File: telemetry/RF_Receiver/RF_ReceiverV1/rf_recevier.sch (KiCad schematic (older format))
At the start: 21 parts, among them J1 USB_B, J3 CONN_02X03, U1 FT231XS, U3 ATmega328P-AU, Y1 Crystal_SMD

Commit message: basic changes to schematic, still more to do
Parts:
- removed C11, C12: C_30pF, footprints:C_0805_OEM, symbol rf_recevier-rescue:C_30pF-formula-benji_arduino2-rescue
- removed C2, C5: C_0.1uF, footprints:C_0805_OEM, symbol rf_recevier-rescue:C_0.1uF-formula-benji_arduino2-rescue
- removed C3: C_100nF, footprints:C_0603_1608Metric, symbol rf_recevier-rescue:C_100nF-formula-benji_arduino2-rescue
- removed D2, D4, D7, D8: LED, symbol Device:LED
- removed F1: F_500mA_16V, footprints:Fuse_1210, symbol rf_recevier-rescue:F_500mA_16V-formula-benji_arduino2-rescue
- removed J1: USB_B, symbol rf_recevier-rescue:USB_B-Connector-benji_arduino2-rescue
- removed J3: CONN_02X03, footprints:Pin_Header_Straight_2x03, symbol rf_recevier-rescue:CONN_02X03-formula-benji_arduino2-rescue
- removed R2, R3, R6, R7, R8, R9: R_1K, footprints:R_0805_OEM, symbol rf_recevier-rescue:R_1K-formula-benji_arduino2-rescue
- removed U1: FT231XS, Package_SO:SSOP-20_3.9x8.7mm_P0.635mm, symbol Interface_USB:FT231XS
- removed U3: ATmega328P-AU, Package_QFP:TQFP-32_7x7mm_P0.8mm, symbol rf_recevier-rescue:ATmega328P-AU-formula-benji_arduino2-rescue
- removed Y1: Crystal_SMD, footprints:Crystal_SMD_FA238, symbol rf_recevier-rescue:Crystal_SMD-formula-benji_arduino2-rescue
- added C? (x2): C_0.1uF, footprints:C_0805_OEM, symbol Formula:C_0.1uF
- added C?: C_100nF, footprints:C_0603_1608Metric, symbol Formula:C_100nF
- added C? (x2): C_30pF, footprints:C_0805_OEM, symbol Formula:C_30pF
- added D?: LED_0805_PB0, footprints:LED_0805_OEM, symbol Formula:LED_0805
- added D? (x2): LED_0805, footprints:LED_0805_OEM, symbol Formula:LED_0805
- added D?: LED_0805_PB5, footprints:LED_0805_OEM, symbol Formula:LED_0805
- added F?: F_500mA_16V, footprints:Fuse_1210, symbol Formula:F_500mA_16V
- added J?: USB_A, symbol Formula:USB_A
- added J?: 0.1in_Female_Socket_01x16, Connector_PinSocket_2.54mm:PinSocket_1x16_P2.54mm_Vertical, symbol Formula:0.1in_Female_Socket_01x16
- added J?: CONN_02X03, footprints:Pin_Header_Straight_2x03, symbol Formula:CONN_02X03
- added R? (x4): R_1K, footprints:R_0805_OEM, symbol Formula:R_1K
- added R? (x2): R_200, footprints:R_0805_OEM, symbol Formula:R_200
- added U?: ATmega328P-AU, Package_QFP:TQFP-32_7x7mm_P0.8mm, symbol Formula:ATmega328P-AU
- added U?: FT232RL, Package_SO:SSOP-28_5.3x10.2mm_P0.65mm, symbol Formula:FT232RL
- added Y?: Crystal_SMD, footprints:Crystal_SMD_FA238, symbol Formula:Crystal_SMD
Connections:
- net labels added: 104, 105, 106, 107, 3v3_FTDI, DEBUG_LED, USB_RX, USB_TX, VBATT
- net labels removed: +5V, 3V3_FTDI, IO4, IO5, IO6, IO7, IO8, Rx, Tx
- wire segments 63 -> 62
- no-connect marks 12 -> 15
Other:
- note added: "LCD Screen Connection"

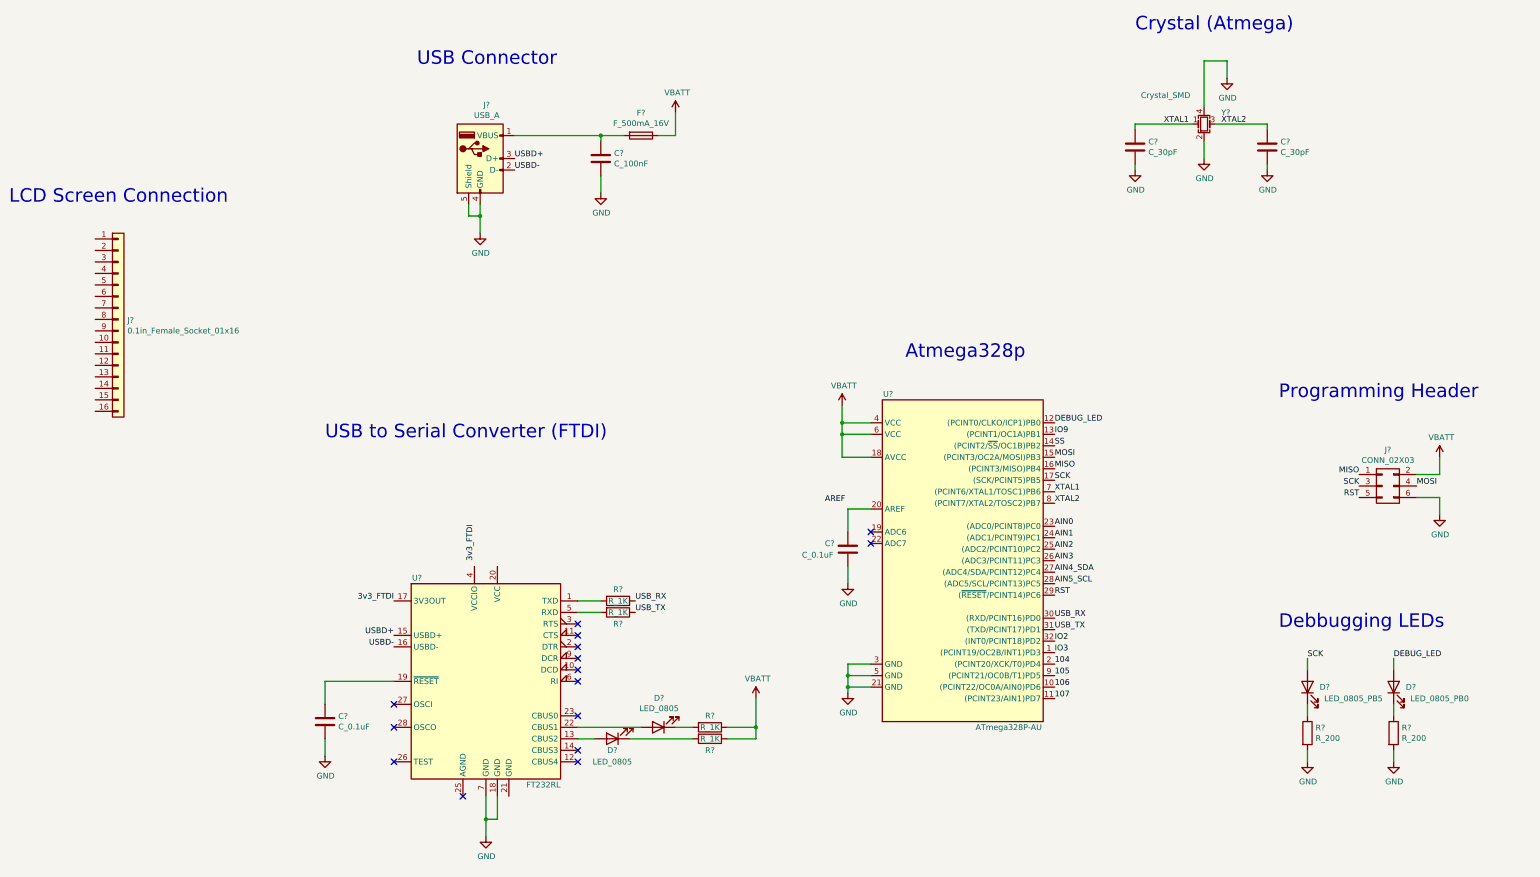
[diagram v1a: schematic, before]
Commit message: added annotations
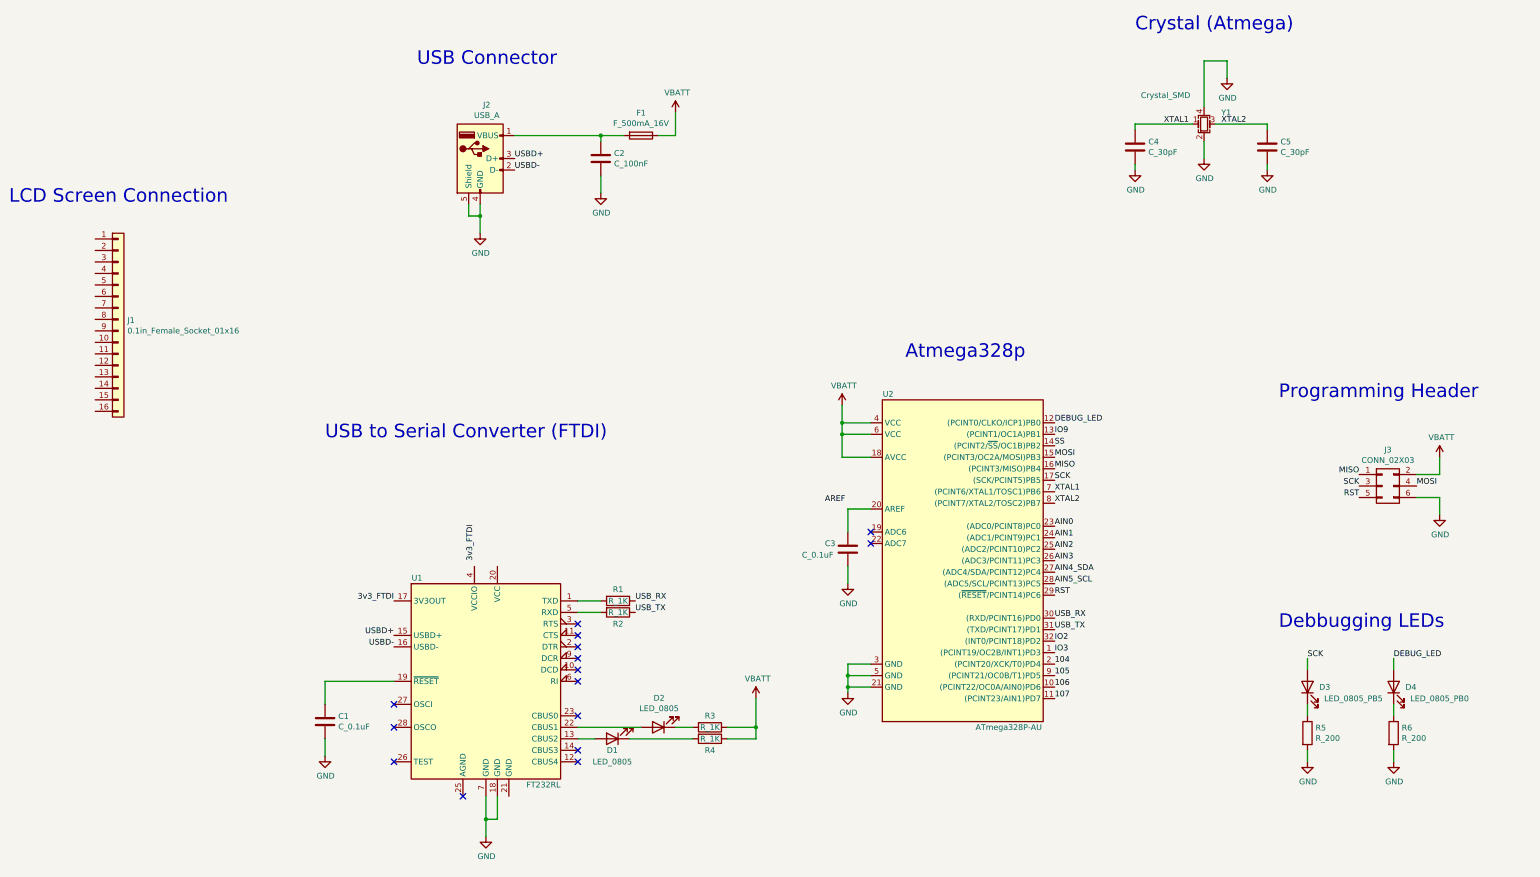
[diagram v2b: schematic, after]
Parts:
- gave numbers to parts that had none: 22
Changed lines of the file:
@@
 USB Connector
 $Comp
-L Formula:FT232RL U?
+L Formula:FT232RL U1
 U 1 1 5FBB1322
 P 5350 7200
-F 0 "U?" H 4750 8100 50  0000 C CNN
+F 0 "U1" H 4750 8100 50  0000 C CNN
 F 1 "FT232RL" H 5850 6300 50  0000 C CNN
 F 2 "Package_SO:SSOP-28_5.3x10.2mm_P0.65mm" H 6450 6300 50  0001 C CNN
@@
 $EndComp
 $Comp
-L Formula:USB_A J?
+L Formula:USB_A J2
 U 1 1 5FBBADA0
 P 5300 2650
-F 0 "J?" H 5357 3117 50  0000 C CNN
+F 0 "J2" H 5357 3117 50  0000 C CNN
 F 1 "USB_A" H 5357 3026 50  0000 C CNN
 F 2 "" H 5450 2600 50  0001 C CNN
@@
 $EndComp
 $Comp
-L Formula:0.1in_Female_Socket_01x16 J?
+L Formula:0.1in_Female_Socket_01x16 J1
 U 1 1 5FBD5439
 P 2150 4050
-F 0 "J?" H 2230 4042 50  0000 L CNN
+F 0 "J1" H 2230 4042 50  0000 L CNN
 F 1 "0.1in_Female_Socket_01x16" H 2230 3951 50  0000 L CNN
 F 2 "Connector_PinSocket_2.54mm:PinSocket_1x16_P2.54mm_Vertical" H 2050 4750 50  0001 C CNN
@@
 $EndComp
 $Comp
-L Formula:CONN_02X03 J?
+L Formula:CONN_02X03 J3
 U 1 1 5FBD8D61
 P 13200 5500
-F 0 "J?" H 13200 5815 50  0000 C CNN
+F 0 "J3" H 13200 5815 50  0000 C CNN
 F 1 "CONN_02X03" H 13200 5724 50  0000 C CNN
 F 2 "footprints:Pin_Header_Straight_2x03" H 13200 4300 50  0001 C CNN
@@
 	3950 7200 3950 7400
 $Comp
-L Formula:VBATT #PWR?
+L Formula:VBATT #PWR07
 U 1 1 5FBF11C9
 P 8450 4800
-F 0 "#PWR?" H 8450 4650 50  0001 C CNN
+F 0 "#PWR07" H 8450 4650 50  0001 C CNN
 F 1 "VBATT" H 8465 4973 50  0000 C CNN
 F 2 "" H 8450 4800 50  0001 C CNN
@@
 	3950 7700 3950 7850
 $Comp
-L power:GND #PWR?
+L power:GND #PWR01
 U 1 1 5FC0F959
 P 3950 7850
-F 0 "#PWR?" H 3950 7600 50  0001 C CNN
+F 0 "#PWR01" H 3950 7600 50  0001 C CNN
 F 1 "GND" H 3955 7677 50  0000 C CNN
 F 2 "" H 3950 7850 50  0001 C CNN
@@
 $EndComp
 $Comp
-L Formula:C_0.1uF C?
+L Formula:C_0.1uF C1
 U 1 1 5FBA02F3
 P 3950 7550
-F 0 "C?" H 4065 7596 50  0000 L CNN
+F 0 "C1" H 4065 7596 50  0000 L CNN
 F 1 "C_0.1uF" H 4065 7505 50  0000 L CNN
 F 2 "footprints:C_0805_OEM" H 3988 7400 50  0001 C CNN
@@
 	8450 5050 8450 4950
 $Comp
-L Formula:VBATT #PWR?
+L Formula:VBATT #PWR06
 U 1 1 5FBCF49A
 P 7700 7350
-F 0 "#PWR?" H 7700 7200 50  0001 C CNN
+F 0 "#PWR06" H 7700 7200 50  0001 C CNN
 F 1 "VBATT" H 7715 7523 50  0000 C CNN
 F 2 "" H 7700 7350 50  0001 C CNN
@@
 3v3_FTDI
 $Comp
-L Formula:R_1K R?
+L Formula:R_1K R3
 U 1 1 5FBDE1F0
 P 7300 7600
-F 0 "R?" V 7200 7600 50  0000 C CNN
+F 0 "R3" V 7200 7600 50  0000 C CNN
 F 1 "R_1K" V 7300 7600 50  0000 C CNN
 F 2 "footprints:R_0805_OEM" H 7230 7600 50  0001 C CNN
@@
 $EndComp
 $Comp
-L Formula:R_1K R?
+L Formula:R_1K R4
 U 1 1 5FBE3B53
 P 7300 7700
-F 0 "R?" V 7400 7700 50  0000 C CNN
+F 0 "R4" V 7400 7700 50  0000 C CNN
 F 1 "R_1K" V 7300 7700 50  0000 C CNN
 F 2 "footprints:R_0805_OEM" H 7230 7700 50  0001 C CNN
@@
 $EndComp
 $Comp
-L Formula:LED_0805 D?
+L Formula:LED_0805 D1
 U 1 1 5FBD99DF
 P 6450 7700
-F 0 "D?" H 6450 7800 50  0000 C CNN
+F 0 "D1" H 6450 7800 50  0000 C CNN
 F 1 "LED_0805" H 6450 7900 50  0000 C CNN
 F 2 "footprints:LED_0805_OEM" H 6350 7700 50  0001 C CNN
@@
 $EndComp
 $Comp
-L Formula:LED_0805 D?
+L Formula:LED_0805 D2
 U 1 1 5FBD7332
 P 6850 7600
-F 0 "D?" H 6843 7345 50  0000 C CNN
+F 0 "D2" H 6843 7345 50  0000 C CNN
 F 1 "LED_0805" H 6843 7436 50  0000 C CNN
 F 2 "footprints:LED_0805_OEM" H 6750 7600 50  0001 C CNN
@@
 	7700 7600 7700 7700
 $Comp
-L Formula:R_1K R?
+L Formula:R_1K R1
 U 1 1 5FC279C9
 P 6500 6500
-F 0 "R?" V 6400 6500 50  0000 C CNN
+F 0 "R1" V 6400 6500 50  0000 C CNN
 F 1 "R_1K" V 6500 6500 50  0000 C CNN
 F 2 "footprints:R_0805_OEM" H 6430 6500 50  0001 C CNN
@@
 $EndComp
 $Comp
-L Formula:R_1K R?
+L Formula:R_1K R2
 U 1 1 5FC279D2
 P 6500 6600
-F 0 "R?" V 6600 6600 50  0000 C CNN
+F 0 "R2" V 6600 6600 50  0000 C CNN
 F 1 "R_1K" V 6500 6600 50  0000 C CNN
 F 2 "footprints:R_0805_OEM" H 6430 6600 50  0001 C CNN
@@
 Connection ~ 5300 3150
 $Comp
-L power:GND #PWR?
+L power:GND #PWR03
 U 1 1 5FC02331
 P 5350 8550
-F 0 "#PWR?" H 5350 8300 50  0001 C CNN
+F 0 "#PWR03" H 5350 8300 50  0001 C CNN
 F 1 "GND" H 5355 8377 50  0000 C CNN
 F 2 "" H 5350 8550 50  0001 C CNN
@@
 $EndComp
 $Comp
-L power:GND #PWR?
+L power:GND #PWR02
 U 1 1 5FC3F217
 P 5300 3300
-F 0 "#PWR?" H 5300 3050 50  0001 C CNN
+F 0 "#PWR02" H 5300 3050 50  0001 C CNN
 F 1 "GND" H 5305 3127 50  0000 C CNN
 F 2 "" H 5300 3300 50  0001 C CNN
@@
 Connection ~ 6350 2450
 $Comp
-L Formula:C_100nF C?
+L Formula:C_100nF C2
 U 1 1 5FC4DEA7
 P 6350 2650
-F 0 "C?" H 6465 2696 50  0000 L CNN
+F 0 "C2" H 6465 2696 50  0000 L CNN
 F 1 "C_100nF" H 6465 2605 50  0000 L CNN
 F 2 "footprints:C_0603_1608Metric" H 6388 2500 50  0001 C CNN
@@
 $EndComp
 $Comp
-L power:GND #PWR?
+L power:GND #PWR04
 U 1 1 5FC4F35A
 P 6350 2950
-F 0 "#PWR?" H 6350 2700 50  0001 C CNN
+F 0 "#PWR04" H 6350 2700 50  0001 C CNN
 F 1 "GND" H 6355 2777 50  0000 C CNN
 F 2 "" H 6350 2950 50  0001 C CNN
@@
 $EndComp
 $Comp
-L Formula:VBATT #PWR?
+L Formula:VBATT #PWR05
 U 1 1 5FC5813F
 P 7000 2250
-F 0 "#PWR?" H 7000 2100 50  0001 C CNN
+F 0 "#PWR05" H 7000 2100 50  0001 C CNN
 F 1 "VBATT" H 7015 2423 50  0000 C CNN
 F 2 "" H 7000 2250 50  0001 C CNN
@@
 $EndComp
 $Comp
-L Formula:F_500mA_16V F?
+L Formula:F_500mA_16V F1
 U 1 1 5FC59506
 P 6700 2450
-F 0 "F?" V 6503 2450 50  0000 C CNN
+F 0 "F1" V 6503 2450 50  0000 C CNN
 F 1 "F_500mA_16V" V 6594 2450 50  0000 C CNN
 F 2 "footprints:Fuse_1210" V 6630 2450 50  0001 C CNN
@@
 	6350 2800 6350 2950
 $Comp
-L power:GND #PWR?
+L power:GND #PWR012
 U 1 1 5FC6FC40
 P 11800 1950
-F 0 "#PWR?" H 11800 1700 50  0001 C CNN
+F 0 "#PWR012" H 11800 1700 50  0001 C CNN
 F 1 "GND" H 11805 1777 50  0000 C CNN
 F 2 "" H 11800 1950 50  0001 C CNN
@@
 $EndComp
 $Comp
-L power:GND #PWR?
+L power:GND #PWR011
 U 1 1 5FC70A2A
 P 11600 2650
-F 0 "#PWR?" H 11600 2400 50  0001 C CNN
+F 0 "#PWR011" H 11600 2400 50  0001 C CNN
 F 1 "GND" H 11605 2477 50  0000 C CNN
 F 2 "" H 11600 2650 50  0001 C CNN
@@
 $EndComp
 $Comp
-L power:GND #PWR?
+L power:GND #PWR010
 U 1 1 5FC71451
 P 11000 2750
-F 0 "#PWR?" H 11000 2500 50  0001 C CNN
+F 0 "#PWR010" H 11000 2500 50  0001 C CNN
 F 1 "GND" H 11005 2577 50  0000 C CNN
 F 2 "" H 11000 2750 50  0001 C CNN
@@
 	11000 2350 11000 2400
 $Comp
-L Formula:C_30pF C?
+L Formula:C_30pF C4
 U 1 1 5FC75CBC
 P 11000 2550
-F 0 "C?" H 11115 2596 50  0000 L CNN
+F 0 "C4" H 11115 2596 50  0000 L CNN
 F 1 "C_30pF" H 11115 2505 50  0000 L CNN
 F 2 "footprints:C_0805_OEM" H 11038 2400 50  0001 C CNN
@@
 	11600 2200 11600 1800
 $Comp
-L Formula:Crystal_SMD Y?
+L Formula:Crystal_SMD Y1
 U 1 1 5FBCF657
 P 11600 2350
-F 0 "Y?" H 11750 2450 50  0000 L CNN
+F 0 "Y1" H 11750 2450 50  0000 L CNN
 F 1 "Crystal_SMD" H 11050 2600 50  0000 L CNN
 F 2 "footprints:Crystal_SMD_FA238" H 11550 2425 50  0001 C CNN
@@
 	11500 2350 11000 2350
 $Comp
-L Formula:C_30pF C?
+L Formula:C_30pF C5
 U 1 1 5FC76DF3
 P 12150 2550
-F 0 "C?" H 12265 2596 50  0000 L CNN
+F 0 "C5" H 12265 2596 50  0000 L CNN
 F 1 "C_30pF" H 12265 2505 50  0000 L CNN
 F 2 "footprints:C_0805_OEM" H 12188 2400 50  0001 C CNN
@@
 	12150 2350 12150 2400
 $Comp
-L power:GND #PWR?
+L power:GND #PWR013
 U 1 1 5FC71E29
 P 12150 2750
-F 0 "#PWR?" H 12150 2500 50  0001 C CNN
+F 0 "#PWR013" H 12150 2500 50  0001 C CNN
 F 1 "GND" H 12155 2577 50  0000 C CNN
 F 2 "" H 12150 2750 50  0001 C CNN
@@
 MOSI
 $Comp
-L Formula:VBATT #PWR?
+L Formula:VBATT #PWR014
 U 1 1 5FC8EFC0
 P 13650 5250
-F 0 "#PWR?" H 13650 5100 50  0001 C CNN
+F 0 "#PWR014" H 13650 5100 50  0001 C CNN
 F 1 "VBATT" H 13665 5423 50  0000 C CNN
 F 2 "" H 13650 5250 50  0001 C CNN
@@
 	13650 5600 13650 5750
 $Comp
-L power:GND #PWR?
+L power:GND #PWR015
 U 1 1 5FC9132A
 P 13650 5750
-F 0 "#PWR?" H 13650 5500 50  0001 C CNN
+F 0 "#PWR015" H 13650 5500 50  0001 C CNN
 F 1 "GND" H 13655 5577 50  0000 C CNN
 F 2 "" H 13650 5750 50  0001 C CNN
@@
 	13450 5600 13650 5600
 $Comp
-L Formula:LED_0805 D?
+L Formula:LED_0805 D4
 U 1 1 5FBD3B41
 P 13250 7250
-F 0 "D?" V 13250 7100 50  0000 C CNN
+F 0 "D4" V 13250 7100 50  0000 C CNN
 F 1 "LED_0805_PB0" V 13150 6850 50  0000 C CNN
 F 2 "footprints:LED_0805_OEM" H 13150 7250 50  0001 C CNN
@@
 $EndComp
 $Comp
-L Formula:LED_0805 D?
+L Formula:LED_0805 D3
 U 1 1 5FCB57F6
 P 12500 7250
-F 0 "D?" V 12500 7100 50  0000 C CNN
+F 0 "D3" V 12500 7100 50  0000 C CNN
 F 1 "LED_0805_PB5" V 12400 6850 50  0000 C CNN
 F 2 "footprints:LED_0805_OEM" H 12400 7250 50  0001 C CNN
@@
 	8500 6200 8500 6350
 $Comp
-L power:GND #PWR?
+L power:GND #PWR08
 U 1 1 5FCD46B7
 P 8500 6350
-F 0 "#PWR?" H 8500 6100 50  0001 C CNN
+F 0 "#PWR08" H 8500 6100 50  0001 C CNN
 F 1 "GND" H 8505 6177 50  0000 C CNN
 F 2 "" H 8500 6350 50  0001 C CNN
@@
 $EndComp
 $Comp
-L Formula:C_0.1uF C?
+L Formula:C_0.1uF C3
 U 1 1 5FCD46C0
 P 8500 6050
-F 0 "C?" H 8300 6100 50  0000 L CNN
+F 0 "C3" H 8300 6100 50  0000 L CNN
 F 1 "C_0.1uF" H 8100 6000 50  0000 L CNN
 F 2 "footprints:C_0805_OEM" H 8538 5900 50  0001 C CNN
@@
 $EndComp
 $Comp
-L power:GND #PWR?
+L power:GND #PWR09
 U 1 1 5FCD90A5
 P 8500 7300
-F 0 "#PWR?" H 8500 7050 50  0001 C CNN
+F 0 "#PWR09" H 8500 7050 50  0001 C CNN
 F 1 "GND" H 8505 7127 50  0000 C CNN
 F 2 "" H 8500 7300 50  0001 C CNN
@@
 $EndComp
 $Comp
-L Formula:ATmega328P-AU U?
+L Formula:ATmega328P-AU U2
 U 1 1 5FBA5FE4
 P 9700 6150
-F 0 "U?" H 8850 7600 50  0000 C CNN
+F 0 "U2" H 8850 7600 50  0000 C CNN
 F 1 "ATmega328P-AU" H 9900 4700 50  0000 C CNN
 F 2 "Package_QFP:TQFP-32_7x7mm_P0.8mm" H 9500 7700 50  0001 C CIN
@@
 XTAL1
 $Comp
-L Formula:R_200 R?
+L Formula:R_200 R5
 U 1 1 5FD1F668
 P 12500 7650
-F 0 "R?" H 12570 7696 50  0000 L CNN
+F 0 "R5" H 12570 7696 50  0000 L CNN
 F 1 "R_200" H 12570 7605 50  0000 L CNN
 F 2 "footprints:R_0805_OEM" H 12430 7650 50  0001 C CNN
@@
 $EndComp
 $Comp
-L Formula:R_200 R?
+L Formula:R_200 R6
 U 1 1 5FD2117A
 P 13250 7650
-F 0 "R?" H 13320 7696 50  0000 L CNN
+F 0 "R6" H 13320 7696 50  0000 L CNN
 F 1 "R_200" H 13320 7605 50  0000 L CNN
 F 2 "footprints:R_0805_OEM" H 13180 7650 50  0001 C CNN

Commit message: fixed libraries
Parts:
- C1, C3: symbol Formula:C_0.1uF -> formula:C_0.1uF
- C2: symbol Formula:C_100nF -> formula:C_100nF
- C4, C5: symbol Formula:C_30pF -> formula:C_30pF
- D1, D2, D3, D4: symbol Formula:LED_0805 -> formula:LED_0805
- F1: symbol Formula:F_500mA_16V -> formula:F_500mA_16V
- J1: symbol Formula:0.1in_Female_Socket_01x16 -> formula:0.1in_Female_Socket_01x16
- J2: symbol Formula:USB_A -> formula:USB_A
- J3: symbol Formula:CONN_02X03 -> formula:CONN_02X03
- R1, R2, R3, R4: symbol Formula:R_1K -> formula:R_1K
- R5, R6: symbol Formula:R_200 -> formula:R_200
- U1: symbol Formula:FT232RL -> formula:FT232RL
- U2: symbol Formula:ATmega328P-AU -> formula:ATmega328P-AU
- Y1: symbol Formula:Crystal_SMD -> formula:Crystal_SMD
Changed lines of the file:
@@
 USB Connector
 $Comp
-L Formula:FT232RL U1
+L formula:FT232RL U1
 U 1 1 5FBB1322
 P 5350 7200
@@
 $EndComp
 $Comp
-L Formula:USB_A J2
+L formula:USB_A J2
 U 1 1 5FBBADA0
 P 5300 2650
@@
 $EndComp
 $Comp
-L Formula:0.1in_Female_Socket_01x16 J1
+L formula:0.1in_Female_Socket_01x16 J1
 U 1 1 5FBD5439
 P 2150 4050
@@
 $EndComp
 $Comp
-L Formula:CONN_02X03 J3
+L formula:CONN_02X03 J3
 U 1 1 5FBD8D61
 P 13200 5500
@@
 	3950 7200 3950 7400
 $Comp
-L Formula:VBATT #PWR07
+L formula:VBATT #PWR07
 U 1 1 5FBF11C9
 P 8450 4800
@@
 $EndComp
 $Comp
-L Formula:C_0.1uF C1
+L formula:C_0.1uF C1
 U 1 1 5FBA02F3
 P 3950 7550
@@
 	8450 5050 8450 4950
 $Comp
-L Formula:VBATT #PWR06
+L formula:VBATT #PWR06
 U 1 1 5FBCF49A
 P 7700 7350
@@
 3v3_FTDI
 $Comp
-L Formula:R_1K R3
+L formula:R_1K R3
 U 1 1 5FBDE1F0
 P 7300 7600
@@
 $EndComp
 $Comp
-L Formula:R_1K R4
+L formula:R_1K R4
 U 1 1 5FBE3B53
 P 7300 7700
@@
 $EndComp
 $Comp
-L Formula:LED_0805 D1
+L formula:LED_0805 D1
 U 1 1 5FBD99DF
 P 6450 7700
@@
 $EndComp
 $Comp
-L Formula:LED_0805 D2
+L formula:LED_0805 D2
 U 1 1 5FBD7332
 P 6850 7600
@@
 	7700 7600 7700 7700
 $Comp
-L Formula:R_1K R1
+L formula:R_1K R1
 U 1 1 5FC279C9
 P 6500 6500
@@
 $EndComp
 $Comp
-L Formula:R_1K R2
+L formula:R_1K R2
 U 1 1 5FC279D2
 P 6500 6600
@@
 Connection ~ 6350 2450
 $Comp
-L Formula:C_100nF C2
+L formula:C_100nF C2
 U 1 1 5FC4DEA7
 P 6350 2650
@@
 $EndComp
 $Comp
-L Formula:VBATT #PWR05
+L formula:VBATT #PWR05
 U 1 1 5FC5813F
 P 7000 2250
@@
 $EndComp
 $Comp
-L Formula:F_500mA_16V F1
+L formula:F_500mA_16V F1
 U 1 1 5FC59506
 P 6700 2450
@@
 	11000 2350 11000 2400
 $Comp
-L Formula:C_30pF C4
+L formula:C_30pF C4
 U 1 1 5FC75CBC
 P 11000 2550
@@
 	11600 2200 11600 1800
 $Comp
-L Formula:Crystal_SMD Y1
+L formula:Crystal_SMD Y1
 U 1 1 5FBCF657
 P 11600 2350
@@
 	11500 2350 11000 2350
 $Comp
-L Formula:C_30pF C5
+L formula:C_30pF C5
 U 1 1 5FC76DF3
 P 12150 2550
@@
 MOSI
 $Comp
-L Formula:VBATT #PWR014
+L formula:VBATT #PWR014
 U 1 1 5FC8EFC0
 P 13650 5250
@@
 	13450 5600 13650 5600
 $Comp
-L Formula:LED_0805 D4
+L formula:LED_0805 D4
 U 1 1 5FBD3B41
 P 13250 7250
@@
 $EndComp
 $Comp
-L Formula:LED_0805 D3
+L formula:LED_0805 D3
 U 1 1 5FCB57F6
 P 12500 7250
@@
 $EndComp
 $Comp
-L Formula:C_0.1uF C3
+L formula:C_0.1uF C3
 U 1 1 5FCD46C0
 P 8500 6050
@@
 $EndComp
 $Comp
-L Formula:ATmega328P-AU U2
+L formula:ATmega328P-AU U2
 U 1 1 5FBA5FE4
 P 9700 6150
@@
 XTAL1
 $Comp
-L Formula:R_200 R5
+L formula:R_200 R5
 U 1 1 5FD1F668
 P 12500 7650
@@
 $EndComp
 $Comp
-L Formula:R_200 R6
+L formula:R_200 R6
 U 1 1 5FD2117A
 P 13250 7650
